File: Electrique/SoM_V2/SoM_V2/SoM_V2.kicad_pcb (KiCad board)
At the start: 6 copper layers, 30 x 60.1 mm, 56 parts, among them Q601 MBT3904DW1T1G, U301 TCA9546APWR, U302 MCP2515-xST, U303 TJA1051T, U304 FT231XS, U401 MCP4822, U402 MCP3202, U501 PCA9633DP1, U602 74HC238, Y301 8MHz

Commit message: push fix ???
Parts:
- removed BOOT: SW_BOOT, Button_Switch_SMD:SW_DIP_SPSTx01_Slide_6.7x4.1mm_W6.73mm_P2.54mm_LowProfile_JPin
- removed C404, C605: 0.1µF, Resistor_SMD:R_0805_2012Metric
- removed C604: 1µF, Resistor_SMD:R_0805_2012Metric
- removed ESP32-S3-MINI-U1: ESP32-S3-MINI-1U, RF_Module:ESP32-S2-MINI-1U
- removed J201: ~, connecteur_M2_key_E:NGFF_E
- removed LED: FZ2812-5050, LED_SMD:LED_Inolux_IN-PI554FCH_PLCC4_5.0x5.0mm_P3.2mm
- removed RESET: SW_CHIP_EN, Button_Switch_SMD:SW_DIP_SPSTx01_Slide_6.7x4.1mm_W6.73mm_P2.54mm_LowProfile_JPin
- removed RX: TX, LED_SMD:LED_0805_2012Metric
- removed TX: RX, LED_SMD:LED_0805_2012Metric
- removed U402: MCP3202, Package_SO:SOIC-8_3.9x4.9mm_P1.27mm
- removed U602: 74HC238, Package_DFN_QFN:DHVQFN-16-1EP_2.5x3.5mm_P0.5mm_EP1x2mm
- added C504: 0.1µF, Resistor_SMD:R_0805_2012Metric, F.Cu at (167.1, 109.2)
- added C505: 0.1µF, Resistor_SMD:R_0805_2012Metric, F.Cu at (167.1, 112.2)
- added D1: GREEN, LED_SMD:LED_0805_2012Metric, F.Cu at (124.3, 104.4)
- added D201: GREEN, LED_SMD:LED_0805_2012Metric, F.Cu at (190.9, 122.8)
- added D301: TX, LED_SMD:LED_0805_2012Metric, F.Cu at (147.6, 104.4)
- added D302: RX, LED_SMD:LED_0805_2012Metric, F.Cu at (147.6, 107.8)
- added D401: FZ2812-5050, LED_SMD:LED_Inolux_IN-PI554FCH_PLCC4_5.0x5.0mm_P3.2mm, F.Cu at (192.6, 116.0)
- added D501: FZ2812-5050, LED_SMD:LED_Inolux_IN-PI554FCH_PLCC4_5.0x5.0mm_P3.2mm, F.Cu at (136.1, 85.6)
- added Q501: MBT3904DW1T1G, Package_TO_SOT_SMD:SOT-363_SC-70-6, F.Cu at (181.9, 117.8)
- added R1: 330, Resistor_SMD:R_0805_2012Metric, F.Cu at (124.3, 102.3)
- added R201: 330, Resistor_SMD:R_0805_2012Metric, F.Cu at (190.8, 125.8)
- added R305: 27, Resistor_SMD:R_0805_2012Metric, F.Cu at (190.8, 100.4)
- added R306: 27, Resistor_SMD:R_0805_2012Metric, F.Cu at (190.8, 103.3)
- added R307: 330, Resistor_SMD:R_0805_2012Metric, F.Cu at (190.8, 106.3)
- added R308: 330, Resistor_SMD:R_0805_2012Metric, F.Cu at (190.8, 109.2)
- added R401: 10k, Resistor_SMD:R_0805_2012Metric, B.Cu at (124.3, 102.3)
- added R402: 10k, Resistor_SMD:R_0805_2012Metric, B.Cu at (124.3, 104.4)
- added R503: 10k, Resistor_SMD:R_0805_2012Metric, F.Cu at (167.1, 121.0)
- added SW501: SW_BOOT, Button_Switch_SMD:SW_DIP_SPSTx01_Slide_6.7x4.1mm_W6.73mm_P2.54mm_LowProfile_JPin, F.Cu at (174.5, 118.8)
- added SW502: SW_CHIP_EN, Button_Switch_SMD:SW_DIP_SPSTx01_Slide_6.7x4.1mm_W6.73mm_P2.54mm_LowProfile_JPin, F.Cu at (174.5, 124.6)
- added SW601: SW_BOOT, Button_Switch_SMD:SW_DIP_SPSTx01_Slide_6.7x4.1mm_W6.73mm_P2.54mm_LowProfile_JPin, F.Cu at (123.7, 84.1)
- added SW602: SW_CHIP_EN, Button_Switch_SMD:SW_DIP_SPSTx01_Slide_6.7x4.1mm_W6.73mm_P2.54mm_LowProfile_JPin, F.Cu at (148.3, 84.0)
- added U201: ~, connecteur_M2_key_E:NGFF_E, F.Cu at (135.8, 139.1)
- added U601: ESP32-S3-MINI-1U, RF_Module:ESP32-S2-MINI-1U, F.Cu at (136.0, 107.0)
- C305, C306, C307, C308, C309, Q601, R602, R603: moved to B.Cu
- C401: value 10µF -> 1µF
- C402: value 0.1µF -> 100nF
- C403: value 10µF -> 100n; footprint Resistor_SMD:R_0805_2012Metric -> Capacitor_SMD:C_0805_2012Metric; moved to F.Cu
- C501: value 1µF -> 10µF; moved to F.Cu
- C502: value 100nF -> 0.1µF; moved to F.Cu
- C503: value 100n -> 1µF; footprint Capacitor_SMD:C_0805_2012Metric -> Resistor_SMD:R_0805_2012Metric; moved to F.Cu
- C606, C607, R301, R302, R313, R316, R501, R502: moved to F.Cu
- U401: value MCP4822 -> PCA9633DP1; footprint Package_SO:SOIC-8_3.9x4.9mm_P1.27mm -> Package_DFN_QFN:DFN-8-1EP_2x2mm_P0.5mm_EP0.9x1.6mm; moved to B.Cu
- U501: value PCA9633DP1 -> ESP32-S3-MINI-1U; footprint Package_DFN_QFN:DFN-8-1EP_2x2mm_P0.5mm_EP0.9x1.6mm -> RF_Module:ESP32-S2-MINI-1U
- moved U501 54.2 mm to (178.2, 107.4)
- moved C501 45.1 mm to (167.1, 100.4), turned to 0 degrees
- moved R502 44.7 mm to (167.1, 118.1), turned to 0 degrees
- moved C502 43.2 mm to (167.1, 103.3), turned to 0 degrees
- moved R501 41.8 mm to (167.1, 115.1), turned to 0 degrees
- moved C503 37.4 mm to (167.1, 106.3), turned to 0 degrees
- moved C403 31.3 mm to (136.0, 89.5), turned to 180 degrees
- moved C307 25.9 mm to (123.0, 118.8), turned to 90 degrees
- moved Y301 25.3 mm to (124.7, 112.9), turned to 0 degrees
- moved U302 24.6 mm to (124.9, 118.8)
- moved C306 23.9 mm to (124.9, 118.8), turned to 90 degrees
- moved C305 22.2 mm to (126.8, 118.8), turned to 90 degrees
- moved C304 22.1 mm to (122.6, 109.2), turned to 90 degrees
- moved R304 21.5 mm to (128.7, 118.8)
- moved C607 21.4 mm to (144.8, 84.0)
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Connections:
- C401 pad 1: GND -> Vcc_3V3
- C401 pad 2: Vcc_3V3 -> GND
- C402 pad 1: GND -> Vcc_3V3
- C402 pad 2: Vcc_3V3 -> GND
- C503 pad 1: Vcc_3V3 -> CHIP_EN
- R501 pad 2: I2C_SDA_ESP32 -> CHIP_EN
- R502 pad 1: Vcc_3V3 -> DTR
- R502 pad 2: I2C_SCL_ESP32 -> Net-(Q501A-B1)
- U303 pad 3: Vcc_3V3 -> Vcc_5V
- U303 pad 5: unconnected-(U303-NC-Pad5) -> Vcc_3V3
- U401 pad 1: Vcc_3V3 -> Net-(U201I-PWM_1_PCA)
- U401 pad 2: SPI_DAC_ESP32 -> Net-(U201I-PWM_2_PCA)
- U401 pad 3: SPI_CLK_ESP32 -> Net-(U201I-PWM_3_PCA)
- U401 pad 4: SPI_MOSI_ESP32 -> Net-(U201I-PWM_4_PCA)
- U401 pad 5: LDAC_DAC -> GND
- U401 pad 6: Net-(J201I-DAC_2_MCP48) -> I2C_SCL_ESP32
- U401 pad 7: GND -> I2C_SDA_ESP32
- U401 pad 8: Net-(J201I-DAC_1_MCP48) -> Vcc_3V3
- U501 pad 1: Net-(J201J-PWM_1_PCA) -> GND
- U501 pad 2: Net-(J201J-PWM_2_PCA) -> GND
- U501 pad 3: Net-(J201J-PWM_3_PCA) -> Vcc_3V3
- U501 pad 4: Net-(J201J-PWM_4_PCA) -> GPIO0_BOOT
- U501 pad 5: GND -> I2C_SDA_ESP32
- U501 pad 7: I2C_SDA_ESP32 -> unconnected-(U501-IO3-Pad7)
- U501 pad 8: Vcc_3V3 -> SPI_CAN_ESP32
- U501 pad 9: (no net) -> CS_1
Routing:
- net Vcc_3V3: track 89.9 -> 15.0 mm, vias 30 -> 2
- net CHIP_EN: track 75.2 -> 10.6 mm, vias 3 -> 1
- net GND: track 118.4 -> 54.1 mm, vias 121 -> 10
- net SPI_CLK_ESP32: track 60.3 -> 2.81 mm, vias 5 -> 1
- net GPIO48/CAN_INT: track 54.9 -> 0.00 mm, vias 2 -> 0
- net GPIO38_ADDRESSABLE_LED: track 56.7 -> 7.22 mm, vias 3 -> 1
- net SPI_MISO_ESP32: track 52.6 -> 3.84 mm, vias 4 -> 1
- net RESET_OTHERS: track 62.6 -> 14.1 mm, vias 5 -> 2
- net SPI_MOSI_ESP32: track 50.9 -> 4.38 mm, vias 2 -> 1
- net I2C_SCL_ESP32: track 59.8 -> 14.6 mm, vias 3 -> 2
- net SPI_5_ESP32: track 42.3 -> 0.00 mm, vias 2 -> 0
- net I2C_SDA_ESP32: track 57.8 -> 15.6 mm, vias 4 -> 0
- net GPIO46: track 42.0 -> 0.00 mm, vias 2 -> 0
- net SPI_6_ESP32: track 41.8 -> 0.00 mm, vias 2 -> 0
- net Net-(J201J-PWM_2_PCA): track 41.5 -> 0.00 mm, vias 2 -> 0
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- removed copper zone on In4.Cu, net GND
- removed copper zone on In3.Cu, net Vcc_3V3
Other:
- copper layers 6 -> 4
- board text removed: "Créé par: Jacob Turcotte Pour: Biogénius SoMV2"
- board text removed: "Si tu lis ça, c'est que tu as mal branché le SoM!"

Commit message: push v2.2
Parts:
- removed C601: 10µF, Resistor_SMD:R_0805_2012Metric
- removed C602, C606, C607: 0.1µF, Resistor_SMD:R_0805_2012Metric
- removed C603: 1µF, Resistor_SMD:R_0805_2012Metric
- removed D1: GREEN, LED_SMD:LED_0805_2012Metric
- removed D501: FZ2812-5050, LED_SMD:LED_Inolux_IN-PI554FCH_PLCC4_5.0x5.0mm_P3.2mm
- removed Q601: MBT3904DW1T1G, Package_TO_SOT_SMD:SOT-363_SC-70-6
- removed R1, R313, R316: 330, Resistor_SMD:R_0805_2012Metric
- removed R601, R602, R603: 10k, Resistor_SMD:R_0805_2012Metric
- removed REF**: MountingHole_3.2mm_M3, MountingHole:MountingHole_3.2mm_M3
- removed SW601: SW_BOOT, Button_Switch_SMD:SW_DIP_SPSTx01_Slide_6.7x4.1mm_W6.73mm_P2.54mm_LowProfile_JPin
- removed SW602: SW_CHIP_EN, Button_Switch_SMD:SW_DIP_SPSTx01_Slide_6.7x4.1mm_W6.73mm_P2.54mm_LowProfile_JPin
- removed U303: TJA1051T, Package_SO:SOIC-8_3.9x4.9mm_P1.27mm
- removed U304: FT231XS, Package_SO:SSOP-20_3.9x8.7mm_P0.635mm
- removed U601: ESP32-S3-MINI-1U, RF_Module:ESP32-S2-MINI-1U
- removed Y301: 8MHz, Crystal:Crystal_SMD_Abracon_ABM3-2Pin_5.0x3.2mm
- added D303: SP0502BAJT, Package_TO_SOT_SMD:SOT-323_SC-70, F.Cu at (124.4, 130.6)
- added R311: 60, Resistor_SMD:R_0805_2012Metric, F.Cu at (126.4, 127.2)
- added R312: 60, Resistor_SMD:R_0805_2012Metric, F.Cu at (122.4, 127.2)
- added U305: SN65HVD230, Package_SO:SOIC-8_3.9x4.9mm_P1.27mm, F.Cu at (124.2, 121.7)
- C303: value 22pF -> 1µF
- C304: value 22pF -> 0.1µF; moved to B.Cu
- C305: value 10µF -> 1µF
- C310, R303: moved to F.Cu
- C501, C502, C503, C504, C505, Q501, R201, R301, R302, R307, R308, R501: moved to B.Cu
- R304: value 10k -> 1k; moved to F.Cu
- R309: value 27 -> 1k
- R310: value 27 -> 1k; moved to B.Cu
- R401, R402: value 10k -> 1k
- U302: value MCP2515-xST -> FT231XQ; footprint Package_SO:TSSOP-20_4.4x6.5mm_P0.65mm -> Package_DFN_QFN:QFN-20-1EP_4x4mm_P0.5mm_EP2.5x2.5mm
- moved R201 67.9 mm to (127.8, 100.3), turned to 90 degrees
- moved D201 65.8 mm to (127.8, 103.8), turned to 90 degrees
- moved D401 57.9 mm to (136.1, 103.6)
- moved R305 55.3 mm to (142.4, 127.0), turned to 90 degrees
- moved SW501 53.5 mm to (123.7, 102.1), turned to 90 degrees
- moved R306 51.2 mm to (145.4, 127.0), turned to 90 degrees
- moved R307 50.4 mm to (140.8, 100.3), turned to 90 degrees
- moved R308 47.5 mm to (144.2, 100.3), turned to 90 degrees
- moved C504 44.0 mm to (123.7, 102.1), turned to 90 degrees
- moved U501 42.8 mm to (135.9, 114.5)
- moved Q501 35.2 mm to (147.1, 112.6)
- moved SW502 34.5 mm to (148.3, 102.1), turned to 90 degrees
- moved C501 34.0 mm to (134.5, 109.9), turned to -90 degrees
- moved C502 30.4 mm to (137.4, 109.9), turned to -90 degrees
- moved C505 28.6 mm to (138.4, 112.6), turned to 180 degrees
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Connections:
- C303 pad 1: Net-(U302-OSC2) -> Vref_CAN
- C303 pad 2: GND -> Net-(D303-A)
- C304 pad 1: Net-(U302-OSC1) -> /Communication/CAN-
- C307 pad 1: Vcc_3V3 -> GND
- C307 pad 2: GND -> /Communication/CAN+
- R304 pad 1: Vcc_3V3 -> GPIO5/TXD
- R304 pad 2: RESET_OTHERS -> Net-(U305-D)
- R309 pad 1: /Communication/DR- -> GPIO4/RXD
- R309 pad 2: /Communication/D- -> Net-(U305-R)
- R310 pad 1: /Communication/DR+ -> GND
- R310 pad 2: /Communication/D+ -> Net-(U305-Rs)
- U201 pad 3: DEBUG+ -> /Communication/DR+
- U201 pad 34: RESET_OTHERS -> unconnected-(U201J-RST_OTHER-Pad34)
- U201 pad 46: /Communication/DR- -> DEBUG-
- U201 pad 48: /Communication/DR+ -> DEBUG+
- U201 pad 5: DEBUG- -> /Communication/DR-
- U201 pad 71: Net-(U201D-CAN_H_MCP2515) -> /Communication/CAN+
- U201 pad 73: Net-(U201D-CAN_L_MCP2515) -> /Communication/CAN-
- U302 pad 1: Net-(U302-TXCAN) -> U0TXD
- U302 pad 10: GND -> Vcc_3V3
- U302 pad 11: unconnected-(U302-~{RX1BF}-Pad11) -> Vcc_3V3
- U302 pad 12: unconnected-(U302-~{RX0BF}-Pad12) -> Vcc_3V3
- U302 pad 13: GPIO48/CAN_INT -> GND
- U302 pad 14: SPI_CLK_ESP32 -> unconnected-(U302-CBUS1-Pad14)
- U302 pad 16: SPI_MOSI_ESP32 -> unconnected-(U302-CBUS3-Pad16)
- U302 pad 17: SPI_MISO_ESP32 -> U0RXD
- U302 pad 18: SPI_CAN_ESP32 -> DTR
- U302 pad 19: RESET_OTHERS -> RTS
- U302 pad 2: Net-(U302-RXCAN) -> unconnected-(U302-~{RI}-Pad2)
- U302 pad 3: unconnected-(U302-CLKOUT/SOF-Pad3) -> GND
- U302 pad 8: Net-(U302-OSC2) -> /Communication/D+
- U302 pad 9: Net-(U302-OSC1) -> /Communication/D-
- U501 pad 15: RESET_OTHERS -> unconnected-(U501-IO11-Pad15)
- U501 pad 8: SPI_CAN_ESP32 -> GPIO4/RXD
- U501 pad 9: CS_1 -> GPIO5/TXD
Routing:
- net Vcc_3V3: track 15.0 -> 152.0 mm, vias 2 -> 10
- net GND: track 54.1 -> 107.8 mm, vias 10 -> 17
- net CHIP_EN: track 10.6 -> 54.3 mm, vias 1 -> 4
- net GPIO46: track 0.00 -> 34.8 mm, vias 0 -> 2
- net GPIO45: track 6.64 -> 39.4 mm, vias 1 -> 4
- net GPIO38_ADDRESSABLE_LED: track 7.22 -> 39.3 mm, vias 1 -> 3
- net I2C_SDA_ESP32: track 15.6 -> 45.5 mm, vias 0 -> 3
- net GPIO33: track 0.00 -> 29.5 mm, vias 0 -> 2
- net I2C_SCL_ESP32: track 14.6 -> 42.9 mm
- net SPI_CLK_ESP32: track 2.81 -> 27.1 mm, vias 1 -> 2
- net I2S_BCLK: track 7.54 -> 29.1 mm, vias 1 -> 2
- net U0RXD: track 0.00 -> 21.4 mm, vias 0 -> 2
- net SPI_MOSI_ESP32: track 4.38 -> 24.4 mm, vias 1 -> 2
- net U0TXD: track 0.00 -> 19.6 mm
- net GPIO48/CAN_INT: track 0.00 -> 19.6 mm, vias 0 -> 1
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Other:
- board size 30 x 60.1 mm -> 30 x 42.1 mm

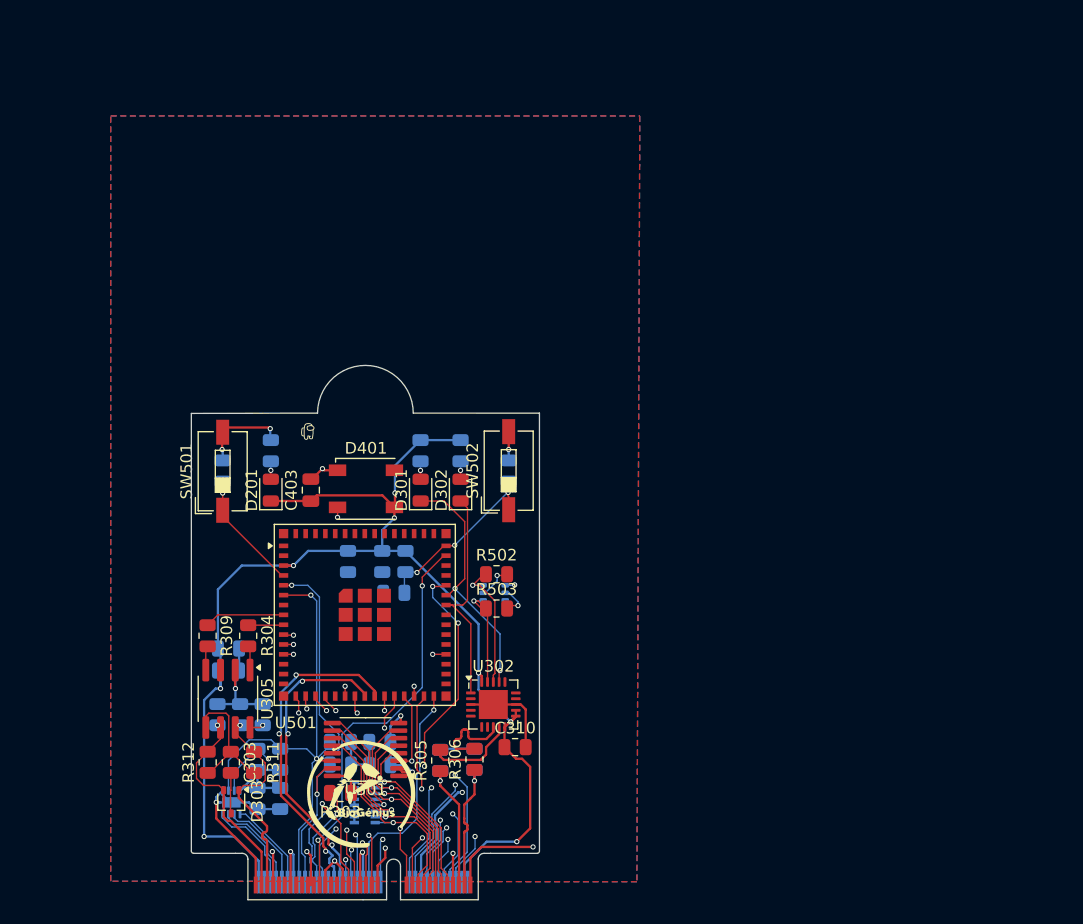
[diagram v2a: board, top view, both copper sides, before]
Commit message: push drc clean up, reste le silkscreen à faire
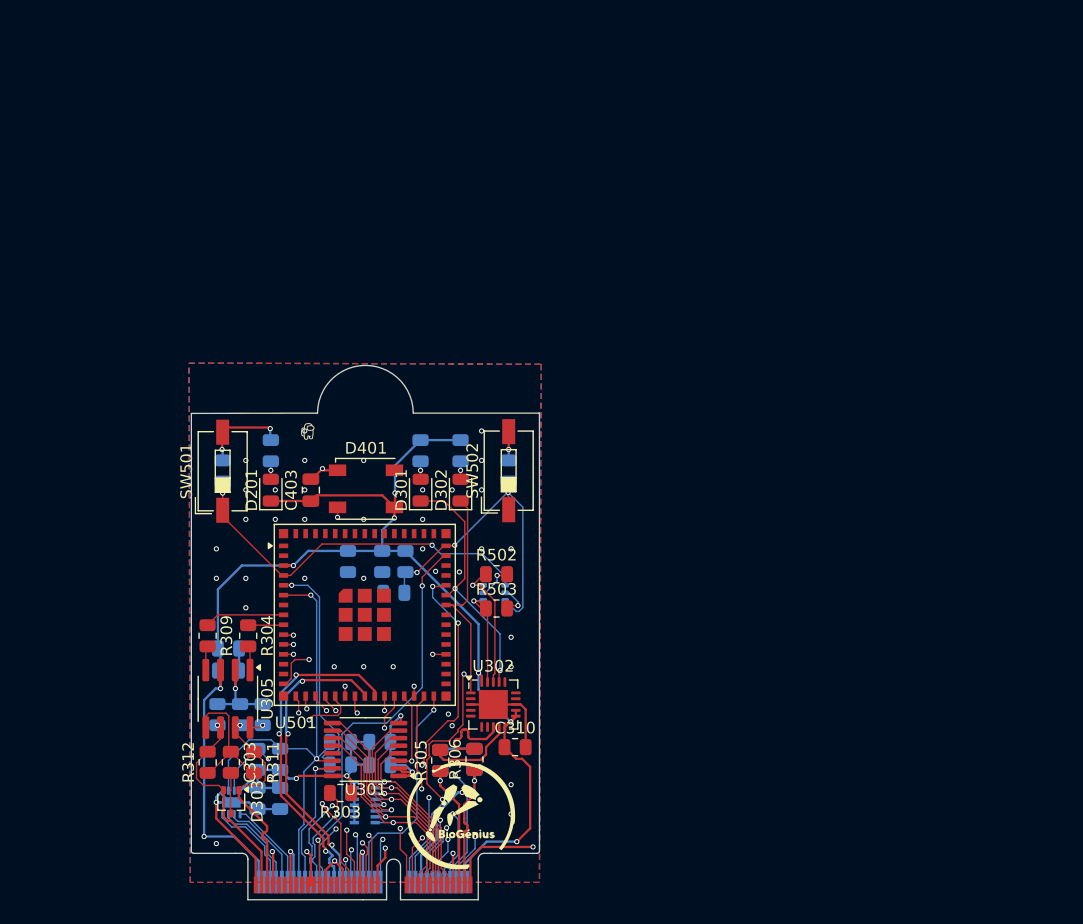
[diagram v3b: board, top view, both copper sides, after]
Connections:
- U501 pad 15: unconnected-(U501-IO11-Pad15) -> CS_1
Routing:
- net CS_1: track 9.93 -> 39.5 mm, vias 1 -> 3
- net GPIO0_BOOT: track 11.2 -> 32.5 mm
- net GPIO16: track 5.01 -> 20.4 mm, vias 1 -> 2
- net CHIP_EN: track 54.3 -> 66.8 mm
- net Vcc_3V3: track 152.0 -> 158.5 mm, vias 10 -> 11
- net I2C_SDA_ESP32: track 45.5 -> 43.4 mm
- net GND: vias 17 -> 55
